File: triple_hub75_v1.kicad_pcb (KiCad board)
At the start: 2 copper layers, 66 x 95.2 mm, 10 parts, among them J1 Conn_02x08_Odd_Even, J2 Raspberry_Pi_2_3, J3 Conn_01x03, J4 Conn_02x08_Odd_Even, J5 Conn_02x08_Odd_Even, U1 74HC245, U2 74HC245, U3 74HC245, U4 74HC245

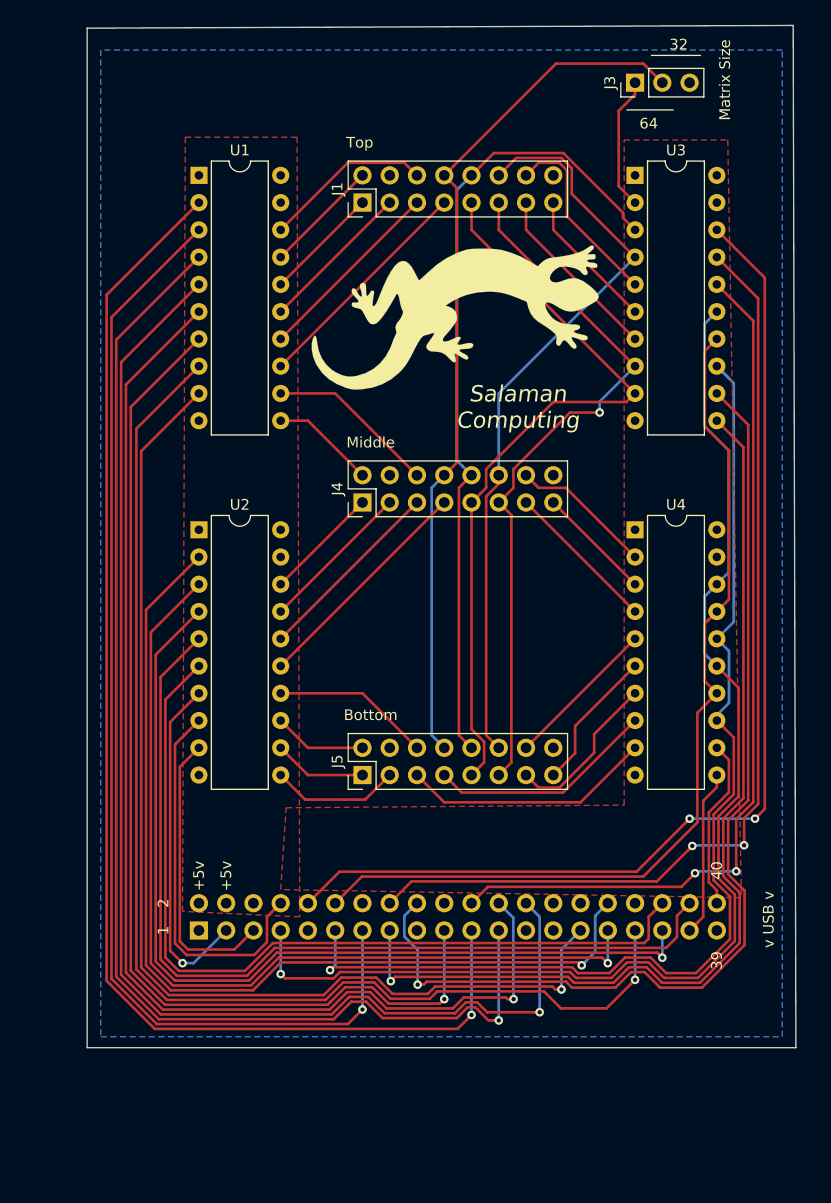
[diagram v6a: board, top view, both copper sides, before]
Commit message: Silkscreen updates and mounting holes
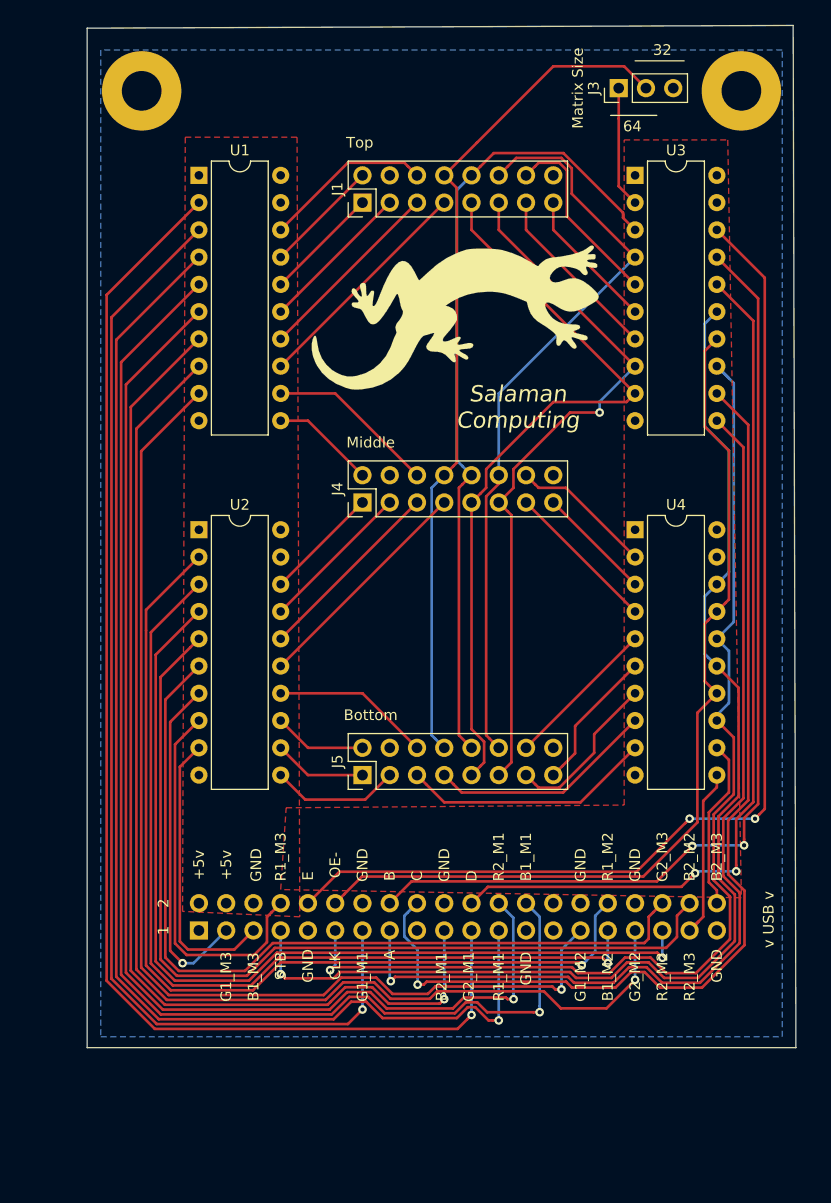
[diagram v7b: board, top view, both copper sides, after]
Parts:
- added REF**: MountingHole_3.7mm_Pad, MountingHole:MountingHole_3.7mm_Pad, F.Cu at (187.7, 25.4)
- added REF**: MountingHole_3.7mm_Pad, MountingHole:MountingHole_3.7mm_Pad, F.Cu at (131.8, 25.4)
- moved J3 1.61 mm to (176.3, 25.1)
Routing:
- net /E: track 80.7 -> 79.1 mm
- net /E_Buff: track 12.4 -> 11.3 mm
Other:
- board text added: "A"
- board text added: "B"
- board text added: "B1_M1"
- board text added: "B1_M2"
- board text added: "B1_M3"
- board text added: "B2_M1"
- board text added: "B2_M2"
- board text added: "B2_M3"
- board text added: "C"
- board text added: "CLK"
- board text added: "D"
- board text added: "E"
- board text added: "G1_M1"
- board text added: "G1_M2"
- board text added: "G1_M3"
- board text added: "G2_M1"
- board text added: "G2_M2"
- board text added: "G2_M3"
- board text added: "GND"
- board text added: "OE-"
- board text added: "R1_M1"
- board text added: "R1_M2"
- board text added: "R1_M3"
- board text added: "R2_M1"
- board text added: "R2_M2"
- board text added: "R2_M3"
- board text added: "STB"
- board text removed: "39"
- board text removed: "40"
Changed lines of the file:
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@@
   (general
     (thickness 1.6)
-    (drawings 21)
-    (tracks 485)
+    (drawings 53)
+    (tracks 484)
     (zones 0)
-    (modules 10)
+    (modules 12)
     (nets 66)
   )
@@
     (add_net "Net-(J2-Pad28)")
   )
+  (module MountingHole:MountingHole_3.7mm_Pad (layer F.Cu)
+    (at 187.706 25.4)
+    (descr "Mounting Hole 3.7mm")
+    (tags "mounting hole 3.7mm")
+    (attr virtual)
+    (fp_text reference REF** (at 0 -4.7) (layer F.SilkS) hide
+      (effects (font (size 1 1) (thickness 0.15)))
+    )
+    (fp_text value MountingHole_3.7mm_Pad (at 0 4.7) (layer F.Fab)
+      (effects (font (size 1 1) (thickness 0.15)))
+    )
+    (fp_circle (center 0 0) (end 3.95 0) (layer F.CrtYd) (width 0.05))
+    (fp_circle (center 0 0) (end 3.7 0) (layer Cmts.User) (width 0.15))
+    (fp_text user %R (at 0.3 0) (layer F.Fab)
+      (effects (font (size 1 1) (thickness 0.15)))
+    )
+    (pad 1 thru_hole circle (at 0 0) (size 7.4 7.4) (drill 3.7) (layers *.Cu *.Mask))
+  )
+  (module MountingHole:MountingHole_3.7mm_Pad (layer F.Cu)
+    (at 131.826 25.4)
+    (descr "Mounting Hole 3.7mm")
+    (tags "mounting hole 3.7mm")
+    (attr virtual)
+    (fp_text reference REF** (at 0 -4.7) (layer F.SilkS) hide
+      (effects (font (size 1 1) (thickness 0.15)))
+    )
+    (fp_text value MountingHole_3.7mm_Pad (at 0 4.7) (layer F.Fab)
+      (effects (font (size 1 1) (thickness 0.15)))
+    )
+    (fp_circle (center 0 0) (end 3.95 0) (layer F.CrtYd) (width 0.05))
+    (fp_circle (center 0 0) (end 3.7 0) (layer Cmts.User) (width 0.15))
+    (fp_text user %R (at 0.3 0) (layer F.Fab)
+      (effects (font (size 1 1) (thickness 0.15)))
+    )
+    (pad 1 thru_hole circle (at 0 0) (size 7.4 7.4) (drill 3.7) (layers *.Cu *.Mask))
+  )
   (module graphics:salamander_silk_1in (layer F.Cu)
     (at 161.036 46.482)
@@
   )
   (module Connector_PinHeader_2.54mm:PinHeader_1x03_P2.54mm_Vertical (layer F.Cu)
-    (at 177.8 24.638 90)
+    (at 176.276 25.146 90)
     (descr "Through hole straight pin header, 1x03, 2.54mm pitch, single row")
     (tags "Through hole pin header THT 1x03 2.54mm single row")
@@
     )
   )
-  (gr_text +5v (at 139.7 98.552 90) (layer F.SilkS)
-    (effects (font (size 1 1) (thickness 0.15)))
-  )
-  (gr_text +5v (at 137.16 98.552 90) (layer F.SilkS)
-    (effects (font (size 1 1) (thickness 0.15)))
-  )
-  (gr_text 40 (at 185.42 98.044 90) (layer F.SilkS)
-    (effects (font (size 1 1) (thickness 0.15)))
-  )
-  (gr_text 39 (at 185.42 106.426 90) (layer F.SilkS)
+  (gr_text R2_M3 (at 182.88 107.95 90) (layer F.SilkS)
+    (effects (font (size 1 1) (thickness 0.15)))
+  )
+  (gr_text R2_M2 (at 180.34 107.95 90) (layer F.SilkS)
+    (effects (font (size 1 1) (thickness 0.15)))
+  )
+  (gr_text G2_M2 (at 177.8 107.95 90) (layer F.SilkS)
+    (effects (font (size 1 1) (thickness 0.15)))
+  )
+  (gr_text B1_M2 (at 175.26 107.95 90) (layer F.SilkS)
+    (effects (font (size 1 1) (thickness 0.15)))
+  )
+  (gr_text G1_M2 (at 172.72 107.95 90) (layer F.SilkS)
+    (effects (font (size 1 1) (thickness 0.15)))
+  )
+  (gr_text GND (at 167.64 107.188 90) (layer F.SilkS)
+    (effects (font (size 1 1) (thickness 0.15)))
+  )
+  (gr_text R1_M1 (at 165.1 107.95 90) (layer F.SilkS)
+    (effects (font (size 1 1) (thickness 0.15)))
+  )
+  (gr_text G2_M1 (at 162.306 107.95 90) (layer F.SilkS)
+    (effects (font (size 1 1) (thickness 0.15)))
+  )
+  (gr_text B2_M1 (at 159.766 107.95 90) (layer F.SilkS)
+    (effects (font (size 1 1) (thickness 0.15)))
+  )
+  (gr_text A (at 154.94 105.918 90) (layer F.SilkS)
+    (effects (font (size 1 1) (thickness 0.15)))
+  )
+  (gr_text G1_M1 (at 152.4 107.95 90) (layer F.SilkS)
+    (effects (font (size 1 1) (thickness 0.15)))
+  )
+  (gr_text CLK (at 149.86 106.934 90) (layer F.SilkS)
+    (effects (font (size 1 1) (thickness 0.15)))
+  )
+  (gr_text GND (at 147.32 106.934 90) (layer F.SilkS)
+    (effects (font (size 1 1) (thickness 0.15)))
+  )
+  (gr_text STB (at 144.78 106.934 90) (layer F.SilkS)
+    (effects (font (size 1 1) (thickness 0.15)))
+  )
+  (gr_text B1_M3 (at 142.24 107.95 90) (layer F.SilkS)
+    (effects (font (size 1 1) (thickness 0.15)))
+  )
+  (gr_text G1_M3 (at 139.7 107.95 90) (layer F.SilkS)
+    (effects (font (size 1 1) (thickness 0.15)))
+  )
+  (gr_text B2_M2 (at 182.88 96.774 90) (layer F.SilkS)
+    (effects (font (size 1 1) (thickness 0.15)))
+  )
+  (gr_text G2_M3 (at 180.34 96.774 90) (layer F.SilkS)
+    (effects (font (size 1 1) (thickness 0.15)))
+  )
+  (gr_text R1_M2 (at 175.26 96.774 90) (layer F.SilkS)
+    (effects (font (size 1 1) (thickness 0.15)))
+  )
+  (gr_text GND (at 177.8 97.536 90) (layer F.SilkS)
+    (effects (font (size 1 1) (thickness 0.15)))
+  )
+  (gr_text GND (at 172.72 97.536 90) (layer F.SilkS)
+    (effects (font (size 1 1) (thickness 0.15)))
+  )
+  (gr_text B1_M1 (at 167.64 96.774 90) (layer F.SilkS)
+    (effects (font (size 1 1) (thickness 0.15)))
+  )
+  (gr_text R2_M1 (at 165.1 96.774 90) (layer F.SilkS)
+    (effects (font (size 1 1) (thickness 0.15)))
+  )
+  (gr_text D (at 162.56 98.552 90) (layer F.SilkS)
+    (effects (font (size 1 1) (thickness 0.15)))
+  )
+  (gr_text GND (at 160.02 97.536 90) (layer F.SilkS)
+    (effects (font (size 1 1) (thickness 0.15)))
+  )
+  (gr_text GND (at 152.4 97.536 90) (layer F.SilkS)
+    (effects (font (size 1 1) (thickness 0.15)))
+  )
+  (gr_text C (at 157.48 98.552 90) (layer F.SilkS)
+    (effects (font (size 1 1) (thickness 0.15)))
+  )
+  (gr_text B (at 154.94 98.552 90) (layer F.SilkS)
+    (effects (font (size 1 1) (thickness 0.15)))
+  )
+  (gr_text OE- (at 149.86 97.536 90) (layer F.SilkS)
+    (effects (font (size 1 1) (thickness 0.15)))
+  )
+  (gr_text E (at 147.32 98.552 90) (layer F.SilkS)
+    (effects (font (size 1 1) (thickness 0.15)))
+  )
+  (gr_text R1_M3 (at 144.78 96.774 90) (layer F.SilkS)
+    (effects (font (size 1 1) (thickness 0.15)))
+  )
+  (gr_text GND (at 142.494 97.536 90) (layer F.SilkS)
+    (effects (font (size 1 1) (thickness 0.15)))
+  )
+  (gr_text +5v (at 139.7 97.536 90) (layer F.SilkS)
+    (effects (font (size 1 1) (thickness 0.15)))
+  )
+  (gr_text +5v (at 137.16 97.536 90) (layer F.SilkS)
+    (effects (font (size 1 1) (thickness 0.15)))
+  )
+  (gr_text B2_M3 (at 185.42 96.774 90) (layer F.SilkS)
+    (effects (font (size 1 1) (thickness 0.15)))
+  )
+  (gr_text GND (at 185.42 106.934 90) (layer F.SilkS)
     (effects (font (size 1 1) (thickness 0.15)))
   )
@@
     (effects (font (size 1 1) (thickness 0.15)))
   )
-  (gr_text "Matrix Size" (at 186.182 24.384 90) (layer F.SilkS)
-    (effects (font (size 1 1) (thickness 0.15)))
-  )
-  (gr_line (start 181.356 27.178) (end 177.038 27.178) (layer F.SilkS) (width 0.12))
-  (gr_line (start 179.324 22.098) (end 183.896 22.098) (layer F.SilkS) (width 0.12))
-  (gr_text 32 (at 181.864 21.082) (layer F.SilkS)
-    (effects (font (size 1 1) (thickness 0.15)))
-  )
-  (gr_text 64 (at 179.07 28.448) (layer F.SilkS)
+  (gr_text "Matrix Size" (at 172.466 25.146 90) (layer F.SilkS)
+    (effects (font (size 1 1) (thickness 0.15)))
+  )
+  (gr_line (start 179.832 27.686) (end 175.514 27.686) (layer F.SilkS) (width 0.12))
+  (gr_line (start 177.8 22.606) (end 182.372 22.606) (layer F.SilkS) (width 0.12))
+  (gr_text 32 (at 180.34 21.59) (layer F.SilkS)
+    (effects (font (size 1 1) (thickness 0.15)))
+  )
+  (gr_text 64 (at 177.546 28.702) (layer F.SilkS)
     (effects (font (size 1 1) (thickness 0.15)))
   )
@@
   (segment (start 159.170001 85.764001) (end 160.02 86.614) (width 0.25) (layer B.Cu) (net 9) (status 30))
   (segment (start 160.02 61.214) (end 158.844999 62.389001) (width 0.25) (layer B.Cu) (net 9) (status 10))
-  (segment (start 160.869999 32.424001) (end 160.02 33.274) (width 0.25) (layer F.Cu) (net 9))
-  (segment (start 170.434 22.86) (end 160.869999 32.424001) (width 0.25) (layer F.Cu) (net 9))
-  (segment (start 178.562 22.86) (end 170.434 22.86) (width 0.25) (layer F.Cu) (net 9))
-  (segment (start 180.34 24.638) (end 178.562 22.86) (width 0.25) (layer F.Cu) (net 9))
+  (segment (start 163.068 30.226) (end 160.02 33.274) (width 0.25) (layer F.Cu) (net 9))
+  (segment (start 176.784 23.114) (end 170.18 23.114) (width 0.25) (layer F.Cu) (net 9))
+  (segment (start 170.18 23.114) (end 163.068 30.226) (width 0.25) (layer F.Cu) (net 9))
+  (segment (start 178.816 25.146) (end 176.784 23.114) (width 0.25) (layer F.Cu) (net 9))
   (segment (start 144.78 51.054) (end 160.02 35.814) (width 0.25) (layer F.Cu) (net 10) (status 30))
   (segment (start 156.630001 32.424001) (end 157.48 33.274) (width 0.25) (layer F.Cu) (net 11) (status 30))
@@
   (segment (start 147.32 89.154) (end 144.78 86.614) (width 0.25) (layer F.Cu) (net 64) (status 20))
   (segment (start 152.4 89.154) (end 147.32 89.154) (width 0.25) (layer F.Cu) (net 64) (status 10))
-  (segment (start 176.276 34.29) (end 176.276 27.262) (width 0.25) (layer F.Cu) (net 65))
-  (segment (start 177.8 25.738) (end 177.8 24.638) (width 0.25) (layer F.Cu) (net 65))
-  (segment (start 176.276 27.262) (end 177.8 25.738) (width 0.25) (layer F.Cu) (net 65))
   (segment (start 177.8 35.814) (end 176.276 34.29) (width 0.25) (layer F.Cu) (net 65))
+  (segment (start 176.276 27.978998) (end 176.276 34.29) (width 0.25) (layer F.Cu) (net 65))
+  (segment (start 176.276 27.978998) (end 176.276 25.146) (width 0.25) (layer F.Cu) (net 65))
   (zone (net 45) (net_name +5V) (layer F.Cu) (hatch edge 0.508)
     (connect_pads (clearance 0.508))

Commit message: Final changes before V1 hits the fab
Gerber files generated,
Mounting holes,
Edge cuts straightened.
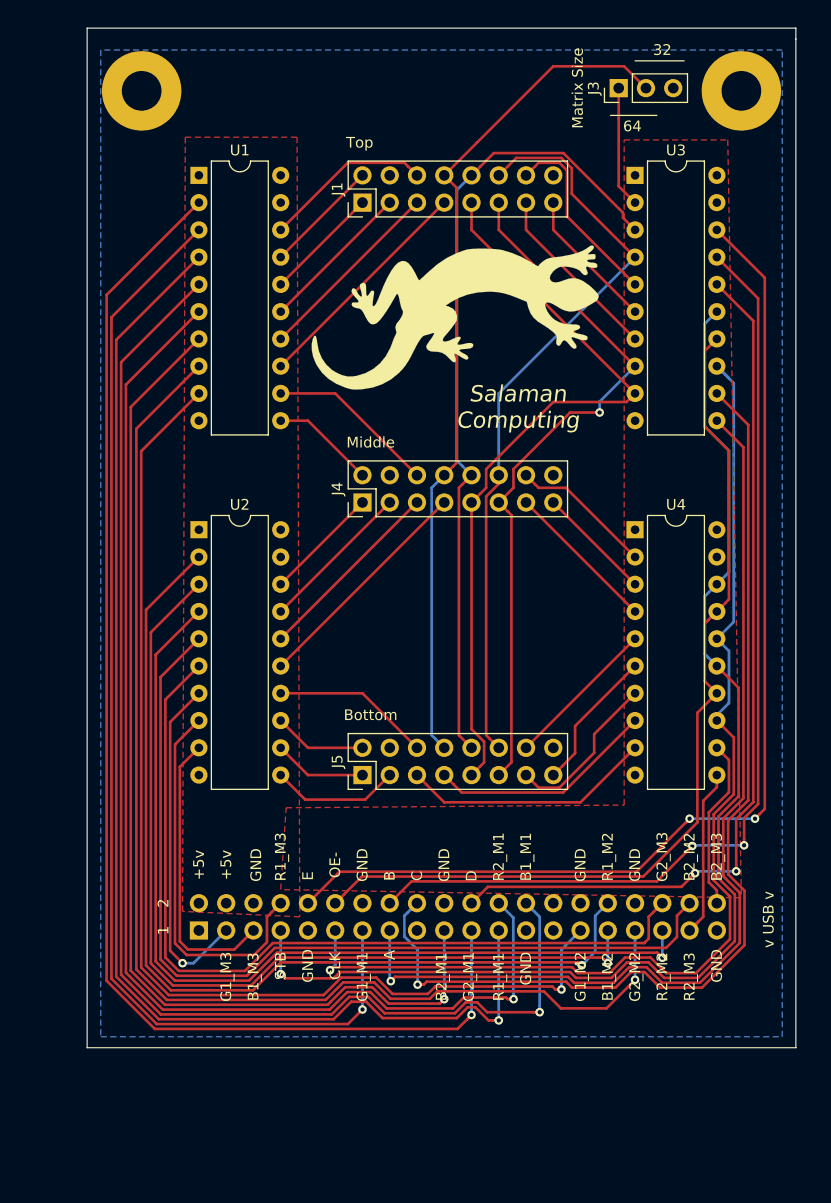
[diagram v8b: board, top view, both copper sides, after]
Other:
- board size 66 x 95.2 mm -> 66 x 95 mm
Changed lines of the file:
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@@
   (general
     (thickness 1.6)
-    (drawings 53)
+    (drawings 54)
     (tracks 484)
     (zones 0)
@@
       (outputformat 1)
       (mirror false)
-      (drillshape 1)
+      (drillshape 0)
       (scaleselection 1)
-      (outputdirectory ""))
+      (outputdirectory "gerber"))
   )
   (net 0 "")
@@
     )
   )
+  (gr_line (start 192.786 19.558) (end 192.786 20.574) (layer Edge.Cuts) (width 0.05))
   (gr_text R2_M3 (at 182.88 107.95 90) (layer F.SilkS)
     (effects (font (size 1 1) (thickness 0.15)))
@@
     (effects (font (size 1 1) (thickness 0.15)))
   )
-  (gr_line (start 192.532 19.304) (end 126.746 19.558) (layer Edge.Cuts) (width 0.05))
-  (gr_line (start 192.786 114.554) (end 192.532 19.304) (layer Edge.Cuts) (width 0.05))
+  (gr_line (start 192.786 19.558) (end 126.746 19.558) (layer Edge.Cuts) (width 0.05))
+  (gr_line (start 192.786 114.554) (end 192.786 20.574) (layer Edge.Cuts) (width 0.05))
   (gr_line (start 126.746 114.554) (end 192.786 114.554) (layer Edge.Cuts) (width 0.05))
   (gr_line (start 126.746 19.558) (end 126.746 114.554) (layer Edge.Cuts) (width 0.05))
